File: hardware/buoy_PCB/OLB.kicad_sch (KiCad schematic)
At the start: 11 parts, among them SW1 SW_Reed

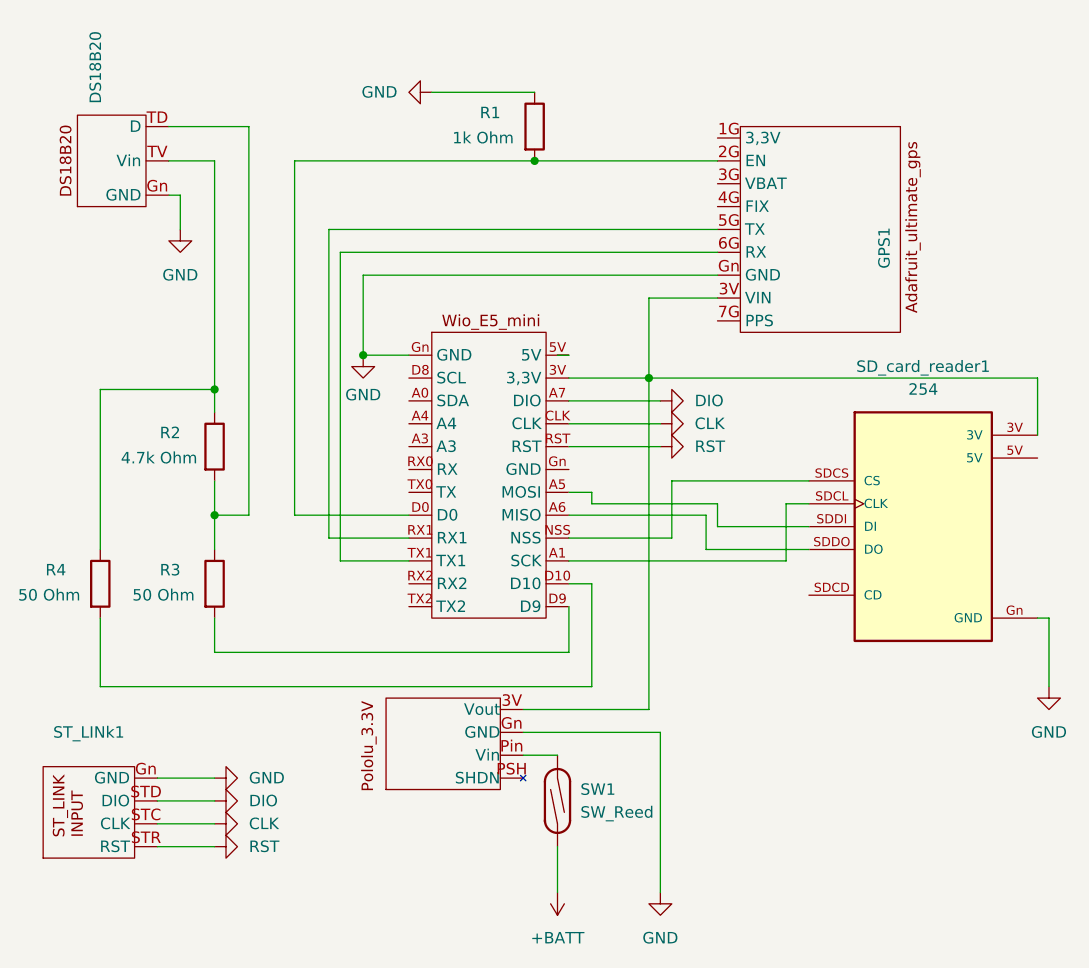
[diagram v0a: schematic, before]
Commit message: Fixed schematic bugs
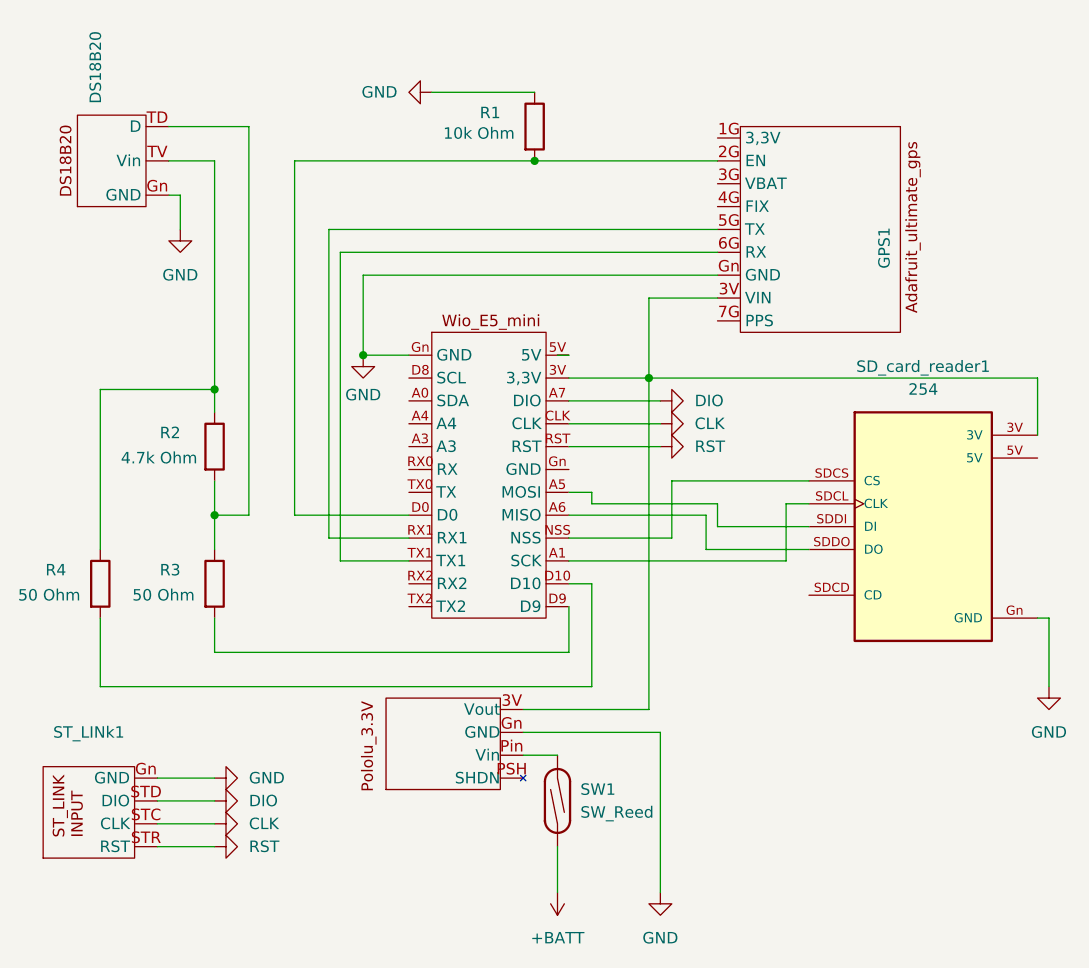
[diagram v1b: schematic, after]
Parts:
- R1: value 1k Ohm -> 10k Ohm
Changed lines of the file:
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@@
 (kicad_sch
-	(version 20231120)
+	(version 20250114)
 	(generator "eeschema")
-	(generator_version "8.0")
+	(generator_version "9.0")
 	(paper "A5")
 	(title_block
@@
 		)
 		(instances
-			(project ""
+			(project "OLB"
 				(path "/de4c88ec-9e47-43f6-ab74-0423293e3d57"
 					(reference "Pololu1")
@@
 			)
 		)
-		(property "Value" "1k Ohm"
-			(at 60.706 34.29 0)
+		(property "Value" "10k Ohm"
+			(at 59.69 33.782 0)
 			(effects
 				(font
@@
 		)
 		(instances
-			(project ""
+			(project "OLB"
 				(path "/de4c88ec-9e47-43f6-ab74-0423293e3d57"
 					(reference "#PWR02")
@@
 		)
 		(instances
-			(project ""
+			(project "OLB"
 				(path "/de4c88ec-9e47-43f6-ab74-0423293e3d57"
 					(reference "Wio1")
@@
 		)
 		(instances
-			(project ""
+			(project "OLB"
 				(path "/de4c88ec-9e47-43f6-ab74-0423293e3d57"
 					(reference "R2")
@@
 		)
 		(instances
-			(project ""
+			(project "OLB"
 				(path "/de4c88ec-9e47-43f6-ab74-0423293e3d57"
 					(reference "ST_LINk1")
@@
 		)
 		(instances
-			(project ""
+			(project "OLB"
 				(path "/de4c88ec-9e47-43f6-ab74-0423293e3d57"
 					(reference "GPS1")
@@
 		)
 		(instances
-			(project ""
+			(project "OLB"
 				(path "/de4c88ec-9e47-43f6-ab74-0423293e3d57"
 					(reference "SD_card_reader1")
@@
 		)
 		(instances
-			(project ""
+			(project "OLB"
 				(path "/de4c88ec-9e47-43f6-ab74-0423293e3d57"
 					(reference "DS18B20")
@@
 		)
 		(instances
-			(project ""
+			(project "OLB"
 				(path "/de4c88ec-9e47-43f6-ab74-0423293e3d57"
 					(reference "#PWR01")
@@
 		)
 		(instances
-			(project ""
+			(project "OLB"
 				(path "/de4c88ec-9e47-43f6-ab74-0423293e3d57"
 					(reference "SW1")
@@
 		)
 	)
+	(embedded_fonts no)
 )
